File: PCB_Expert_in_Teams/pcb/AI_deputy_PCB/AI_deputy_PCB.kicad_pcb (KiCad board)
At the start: 2 copper layers, 110 parts, among them IC1 DA7280-00FVC, IC2 DA7281-00FVC, IC3 DA7282-00FVC, IC4 IS31AP2005-SLS2-TR, IC5 IS31AP2005-SLS2-TR, IC6 LM25576QMH_NOPB, IC7 CYPD3177-24LQXQ, IC8 FT231XS-R, J1 Piezo Electric, J10 OUTPUT Haptic B (Neck R), J11 OUTPUT Haptic C (Back), J12 Haptic Power and GND, J13 Conn_01x02_Socket, J14 Conn_01x02_Socket, J3 Haptic Power and GND, J4 UART, J5 JST CONN from MCU, J6 JTAG, J7 JST CONN from MCU, J8 Conn_01x04_Socket, J9 OUTPUT Haptic A (Neck L), Q1 NMOS, Q2 DMP3098LSD-13, Q4 DMP3098LSD-13, U2 ESP32-WROOM-32UE

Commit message: update schematic from desktop
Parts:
- added C38: 4u7, Capacitor_SMD:C_0805_2012Metric_Pad1.18x1.45mm_HandSolder, F.Cu at (202.5, 19.4)
- added C44: 100n, Capacitor_SMD:C_0805_2012Metric_Pad1.18x1.45mm_HandSolder, F.Cu at (218.5, 20.8)
- added C45: 4u7, Capacitor_SMD:C_0805_2012Metric_Pad1.18x1.45mm_HandSolder, F.Cu at (198.6, 24.3)
- added C46: 100n, Capacitor_SMD:C_0805_2012Metric_Pad1.18x1.45mm_HandSolder, F.Cu at (218.6, 28.7)
- added C47: 4u7, Capacitor_SMD:C_0805_2012Metric_Pad1.18x1.45mm_HandSolder, F.Cu at (250.9, 49.9)
- added C48: 4u7, Capacitor_SMD:C_0805_2012Metric_Pad1.18x1.45mm_HandSolder, F.Cu at (202.5, 25.4)
- added C50: 4u7, Capacitor_SMD:C_0805_2012Metric_Pad1.18x1.45mm_HandSolder, F.Cu at (231.5, 42.3)
- added C50: 4u7, Capacitor_SMD:C_0805_2012Metric_Pad1.18x1.45mm_HandSolder, F.Cu at (202.5, 28.4)
- added C51: 100n, Capacitor_SMD:C_0805_2012Metric_Pad1.18x1.45mm_HandSolder, F.Cu at (226.3, 42.3)
- added C52: 10u, Capacitor_SMD:CP_Elec_4x5.4, F.Cu at (69.2, 117.2)
- added C53: 0.1u, Capacitor_SMD:C_0805_2012Metric_Pad1.18x1.45mm_HandSolder, F.Cu at (75.6, 117.2)
- added C54: 2.2u, Capacitor_SMD:C_0805_2012Metric_Pad1.18x1.45mm_HandSolder, F.Cu at (73.9, 123.3)
- added C55: 2.2u, Capacitor_SMD:C_0805_2012Metric_Pad1.18x1.45mm_HandSolder, F.Cu at (69.3, 123.3)
- added C56: 2.2u, Capacitor_SMD:C_0805_2012Metric_Pad1.18x1.45mm_HandSolder, F.Cu at (64.4, 133.4)
- added C57: 2.2u, Capacitor_SMD:C_0805_2012Metric_Pad1.18x1.45mm_HandSolder, F.Cu at (64.4, 126.6)
- added C58: 10u, Capacitor_SMD:CP_Elec_4x5.4, F.Cu at (88.2, 114.4)
- added C59: 0.1u, Capacitor_SMD:C_0805_2012Metric_Pad1.18x1.45mm_HandSolder, F.Cu at (82.1, 114.9)
- added C6: 10uF, Capacitor_SMD:C_0805_2012Metric_Pad1.18x1.45mm_HandSolder, F.Cu at (209.3, 33.2)
- added C60: 10u, Capacitor_SMD:CP_Elec_4x5.4, F.Cu at (97.4, 120.6)
- added C61: 0.1u, Capacitor_SMD:C_0805_2012Metric_Pad1.18x1.45mm_HandSolder, F.Cu at (90.8, 120.6)
- added IC9: PCM5102APWR, EXT_AI_DEPUTY_Library:SOP65P640X120-20N, F.Cu at (80.3, 124.5)
- added J16: Conn_01x01_Pin, TestPoint:TestPoint_Pad_4.0x4.0mm, F.Cu at (264.0, 33.0)
- added J17: Conn_01x01_Pin, TestPoint:TestPoint_Pad_4.0x4.0mm, F.Cu at (252.0, 33.0)
- added J2: 2171790001, EXT_AI_DEPUTY_Library:MOLEX_2171790001, F.Cu at (234.3, 33.4)
- added R37: R, Resistor_SMD:R_0805_2012Metric_Pad1.20x1.40mm_HandSolder, F.Cu at (217.4, 26.0)
- added R38: 27, Resistor_SMD:R_0805_2012Metric_Pad1.20x1.40mm_HandSolder, F.Cu at (228.1, 20.8)
- added R39: 100k, Resistor_SMD:R_0805_2012Metric_Pad1.20x1.40mm_HandSolder, F.Cu at (208.6, 22.4)
- added R40: 100k, Resistor_SMD:R_0805_2012Metric_Pad1.20x1.40mm_HandSolder, F.Cu at (209.3, 28.2)
- added R41: 10k, Resistor_SMD:R_0805_2012Metric_Pad1.20x1.40mm_HandSolder, F.Cu at (103.8, 120.7)
- added R42: 470, Resistor_SMD:R_0805_2012Metric_Pad1.20x1.40mm_HandSolder, F.Cu at (68.6, 132.5)
- added R43: 470, Resistor_SMD:R_0805_2012Metric_Pad1.20x1.40mm_HandSolder, F.Cu at (68.7, 127.7)
- added S1: 430773034825, EXT_AI_DEPUTY_Library:430773034825, F.Cu at (132.7, 50.0)
- added S2: 430773034825, EXT_AI_DEPUTY_Library:430773034825, F.Cu at (185.9, 48.5)
- C41: value 4u7 -> 0.1u
- C42: value 100n -> 10u; footprint Capacitor_SMD:C_0805_2012Metric_Pad1.18x1.45mm_HandSolder -> Capacitor_SMD:CP_Elec_4x5.4
- moved C41 178.7 mm to (77.2, 132.3), turned to 90 degrees
- moved C1 172.8 mm to (258.6, 86.1)
- moved R3 172.3 mm to (263.4, 86.1)
- moved C42 168.4 mm to (83.9, 132.2)
- moved Q1 153.3 mm to (263.2, 80.6)
- moved R35 126.7 mm to (251.9, 62.4)
- moved C3 118.9 mm to (189.0, 41.8)
- moved R4 104.0 mm to (139.4, 46.3), turned to -90 degrees
- moved R36 89.7 mm to (246.7, 60.6)
- moved D1 82.5 mm to (145.1, 31.5), turned to 180 degrees
- moved R8 74.1 mm to (140.3, 31.5)
- moved C24 72.2 mm to (166.8, 114.4), turned to -90 degrees
- moved C25 69.7 mm to (168.8, 77.2), turned to -90 degrees
- moved C23 69.2 mm to (162.2, 114.4), turned to -90 degrees
- moved C49 67.8 mm to (258.0, 40.4)
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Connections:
- C3 pad 1: Net-(C3-Pad1) -> EN_ESP32
- C41 pad 1: VBUS -> GND
- C41 pad 2: GND -> +3V3
- C42 pad 1: VBUS -> +3V3
- R2 pad 2: Net-(C3-Pad1) -> EN_ESP32
- R35 pad 1: Net-(Q2-G1) -> SAFE_PWR_EN
- R35 pad 2: SAFE_PWR_EN -> Net-(Q2-G1)
- U2 pad 27: unconnected-(U2-IO16-Pad27) -> DAC_LRCK
- U2 pad 28: unconnected-(U2-IO17-Pad28) -> DAC_DIN
- U2 pad 30: unconnected-(U2-IO18-Pad30) -> DAC_BCK
- U2 pad 31: unconnected-(U2-IO19-Pad31) -> PD_INT
- U2 pad 37: unconnected-(U2-IO23-Pad37) -> MUTE
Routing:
- net +3V3: track 276.3 -> 416.9 mm, vias 0 -> 4
- net VBUS: track 13.3 -> 95.7 mm, vias 0 -> 4
- net EN_ESP32: track 0.00 -> 63.5 mm, vias 0 -> 2
- net VDC_OUT: track 0.00 -> 43.6 mm, vias 0 -> 2
- net VBUSEN: track 0.00 -> 37.3 mm, vias 0 -> 2
- net Net-(C47-Pad2): track 0.00 -> 29.7 mm
- net SAFE_PWR_EN: track 0.00 -> 26.5 mm, vias 0 -> 2
- net MUTE: track 0.00 -> 22.2 mm
- net Net-(IC9-CAPP): track 0.00 -> 19.8 mm
- net Net-(Q2-G1): track 0.00 -> 17.6 mm
- net Net-(IC9-LDOO): track 0.00 -> 15.9 mm
- net Net-(IC7-VCCD): track 0.00 -> 14.9 mm
- net Net-(IC5-OUT-): track 0.00 -> 12.9 mm, vias 0 -> 1
- net Net-(IC4-OUT-): track 0.00 -> 12.5 mm, vias 0 -> 1
- net /PD and USBC/CC1: track 0.00 -> 12.5 mm, vias 0 -> 2
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- added copper zone on F.Cu, net VDC_OUT

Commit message: fixed small things, push from laptop
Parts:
- removed the C38 at (216.1, 51.9)
- removed the C45 at (218.6, 60.8)
- removed the C48 at (248.1, 40.5)
- removed the C50 at (231.5, 42.3)
- removed the C6 at (135.8, 36.2)
- R37: value R -> 27
- moved C6 73.4 mm to (136.0, 36.2), turned to -90 degrees
- moved C48 47.8 mm to (248.0, 40.2), turned to 180 degrees
- moved C45 41.9 mm to (218.8, 61.0), turned to -90 degrees
- moved R38 35.3 mm to (201.2, 43.8)
- moved C38 35.2 mm to (216.1, 51.9), turned to -90 degrees
- moved C44 34.1 mm to (204.2, 51.8), turned to -90 degrees
- moved C50 32.1 mm to (231.5, 42.3), turned to -90 degrees
- moved C46 29.3 mm to (200.2, 51.5), turned to -90 degrees
- moved R39 27.6 mm to (197.2, 47.5), turned to 90 degrees
- moved R40 26.4 mm to (196.8, 51.5), turned to 90 degrees
- moved R37 22.4 mm to (201.2, 41.5)
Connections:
- net Net-(IC8-USBDM) renamed -
- net Net-(IC8-USBDP) renamed +
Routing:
- net D+: track 4.36 -> 51.0 mm, vias 1 -> 2
- net D-: track 2.77 -> 48.3 mm, vias 0 -> 2
- net Net-(IC8-3V3OUT): track 0.00 -> 20.3 mm
- net +3V3: track 416.9 -> 433.5 mm
- net Net-(IC8-CBUS3): track 0.00 -> 12.5 mm, vias 0 -> 2
- net +: track 0.00 -> 4.78 mm
- net -: track 0.00 -> 4.53 mm

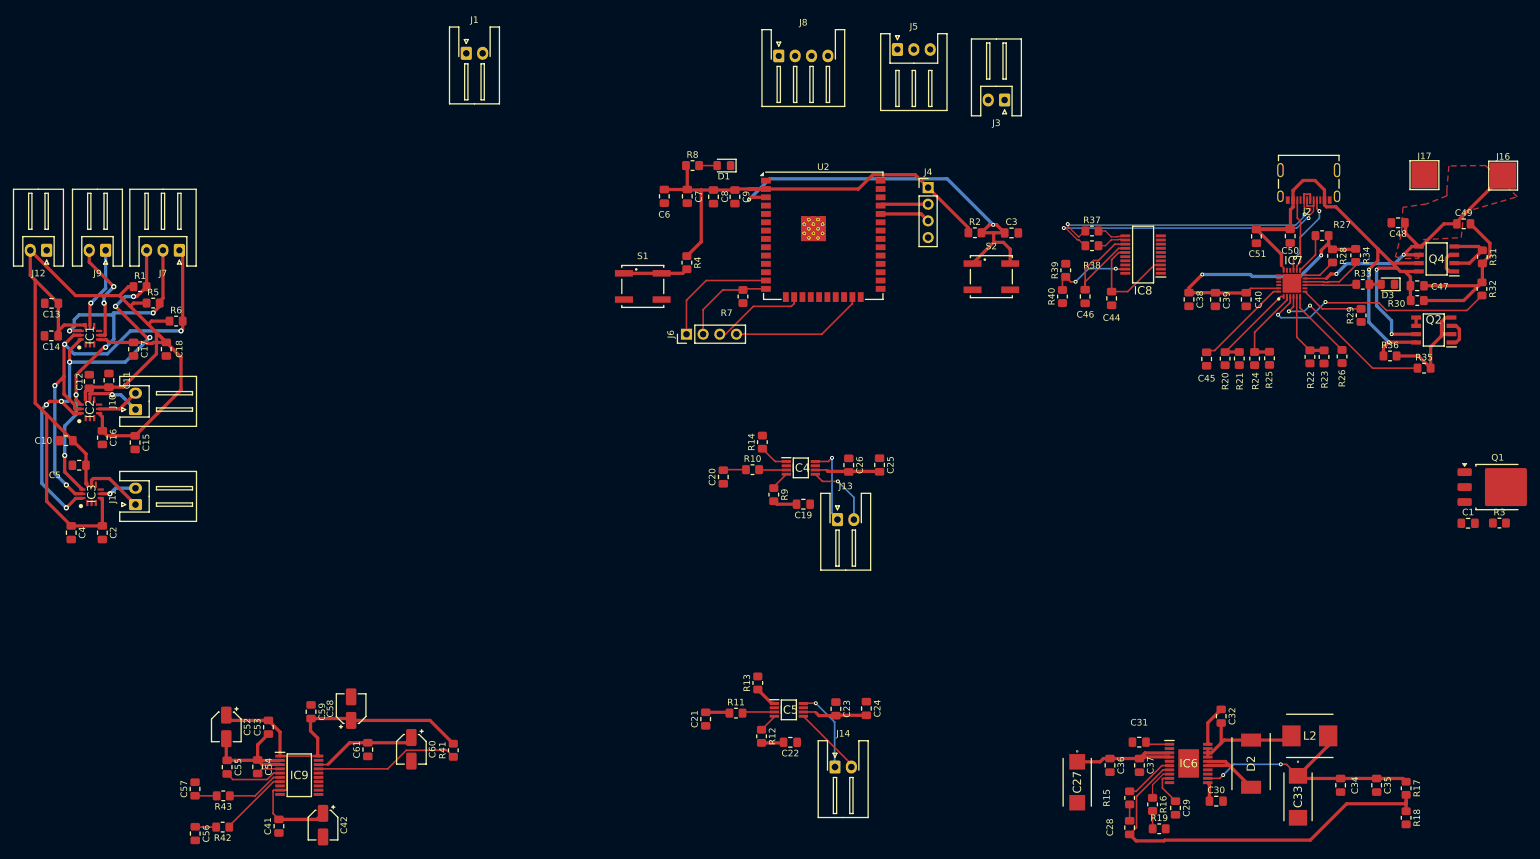
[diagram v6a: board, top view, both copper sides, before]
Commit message: pcb v0.1 plus cad render for mech students
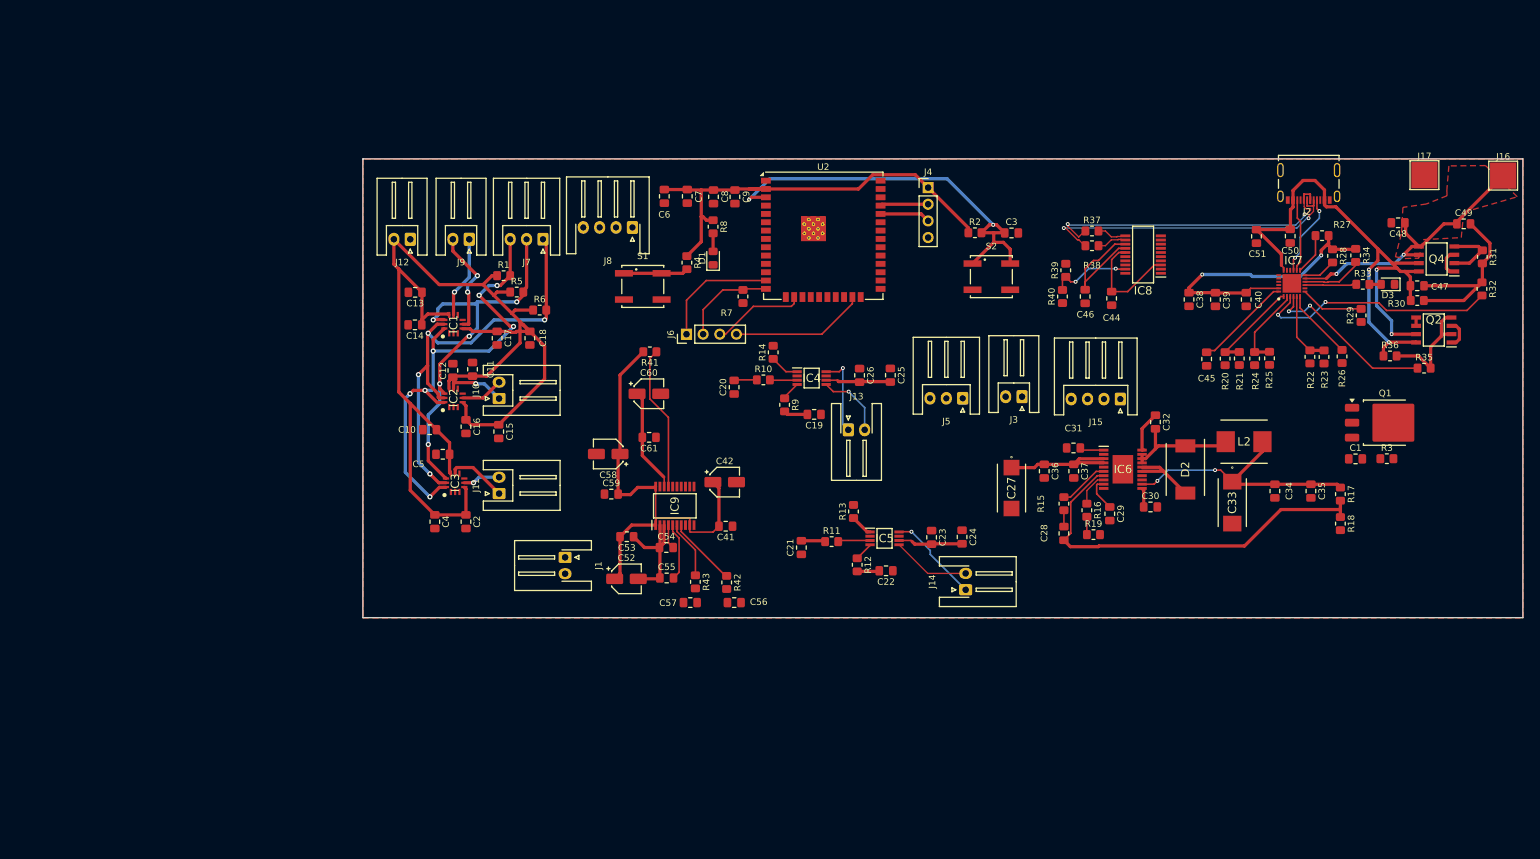
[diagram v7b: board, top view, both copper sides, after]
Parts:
- added J15: Conn_01x04_Socket, Connector_JST:JST_XH_S4B-XH-A_1x04_P2.50mm_Horizontal, F.Cu at (205.6, 67.1)
- moved C56 89.5 mm to (146.7, 98.2), turned to 0 degrees
- moved R42 85.5 mm to (145.5, 95.1), turned to -90 degrees
- moved C41 82.1 mm to (145.4, 86.5), turned to 180 degrees
- moved C57 80.7 mm to (140.0, 98.2), turned to 180 degrees
- moved C42 80.6 mm to (145.2, 79.8), turned to 0 degrees
- moved R43 79.1 mm to (140.7, 95.0), turned to -90 degrees
- moved J1 78.4 mm to (120.9, 91.3), turned to -90 degrees
- moved C55 73.0 mm to (136.4, 94.5), turned to 0 degrees
- moved C54 70.8 mm to (136.3, 89.8), turned to 0 degrees
- moved IC9 70.5 mm to (137.6, 83.4), turned to 90 degrees
- moved R41 67.8 mm to (133.8, 59.9), turned to 180 degrees
- moved C60 65.2 mm to (133.6, 66.3), turned to 0 degrees
- moved C52 65.1 mm to (130.2, 94.6), turned to 0 degrees
- moved C61 64.1 mm to (133.7, 73.0), turned to 180 degrees
- moved C53 61.9 mm to (130.3, 88.2), turned to 180 degrees
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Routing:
- net Signal Left: track 3.31 -> 0.00 mm
- net Signal Right: track 3.21 -> 0.00 mm
- net +3V3: track 433.5 -> 431.8 mm
- net Net-(IC5-OUT-): track 12.9 -> 14.2 mm
- net Net-(IC5-OUT+): track 10.8 -> 12.0 mm
- added copper zone on B.Cu, net GND
- added copper zone on F.Cu, net GND
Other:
- board outline added: 177 x 70 mm

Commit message: update after lab session with gustav saturday
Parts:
- removed C60: 10u, Capacitor_SMD:CP_Elec_4x5.4
- removed C61: 0.1u, Capacitor_SMD:C_0805_2012Metric_Pad1.18x1.45mm_HandSolder
- removed J12: Haptic Power and GND, Connector_JST:JST_XH_S2B-XH-A_1x02_P2.50mm_Horizontal
- removed J7: JST CONN from MCU, Connector_JST:JST_XH_S3B-XH-A_1x03_P2.50mm_Horizontal
- added D1: LED, LED_SMD:LED_0805_2012Metric_Pad1.15x1.40mm_HandSolder, F.Cu at (207.7, 147.9)
- added J18: Conn_01x03_Socket, Connector_PinHeader_2.54mm:PinHeader_1x03_P2.54mm_Vertical, F.Cu at (190.4, 156.9)
- added J19: Conn_01x01_Pin, TestPoint:TestPoint_Pad_4.0x4.0mm, F.Cu at (191.1, 143.5)
- added J20: Conn_01x01_Pin, TestPoint:TestPoint_Pad_4.0x4.0mm, F.Cu at (191.1, 149.6)
- added JP1: SolderJumper_2_Open, Jumper:SolderJumper-2_P1.3mm_Open_RoundedPad1.0x1.5mm, F.Cu at (203.1, 142.3)
- added JP2: SolderJumper_2_Open, Jumper:SolderJumper-2_P1.3mm_Open_RoundedPad1.0x1.5mm, F.Cu at (203.1, 145.8)
- added R44: 330, Resistor_SMD:R_0805_2012Metric_Pad1.20x1.40mm_HandSolder, F.Cu at (203.3, 152.9)
- added R45: 330, Resistor_SMD:R_0805_2012Metric_Pad1.20x1.40mm_HandSolder, F.Cu at (203.3, 155.8)
- added R46: 330, Resistor_SMD:R_0805_2012Metric_Pad1.20x1.40mm_HandSolder, F.Cu at (203.3, 158.8)
- added R47: 68, Resistor_SMD:R_0805_2012Metric_Pad1.20x1.40mm_HandSolder, F.Cu at (207.6, 144.9)
- added R48: 330, Resistor_SMD:R_0805_2012Metric_Pad1.20x1.40mm_HandSolder, F.Cu at (197.5, 135.9)
- added R49: 430, Resistor_SMD:R_0805_2012Metric_Pad1.20x1.40mm_HandSolder, F.Cu at (195.1, 156.1)
- added R50: 200, Resistor_SMD:R_0805_2012Metric_Pad1.20x1.40mm_HandSolder, F.Cu at (195.1, 159.0)
- added R51: 430, Resistor_SMD:R_0805_2012Metric_Pad1.20x1.40mm_HandSolder, F.Cu at (104.0, 136.2)
- added R52: 430, Resistor_SMD:R_0805_2012Metric_Pad1.20x1.40mm_HandSolder, F.Cu at (99.0, 136.9)
- added R53: 3.3k, Resistor_SMD:R_0805_2012Metric_Pad1.20x1.40mm_HandSolder, F.Cu at (103.5, 67.3)
- added R54: 3.3k, Resistor_SMD:R_0805_2012Metric_Pad1.20x1.40mm_HandSolder, F.Cu at (103.5, 70.2)
- added R55: 3.3k, Resistor_SMD:R_0805_2012Metric_Pad1.20x1.40mm_HandSolder, F.Cu at (103.5, 73.2)
- added R8: 10k, Resistor_SMD:R_0805_2012Metric_Pad1.20x1.40mm_HandSolder, F.Cu at (207.6, 142.0)
- C1: value 100u -> 10u
- C56, C57: value 2.2u -> 2.2n; footprint Capacitor_SMD:C_0805_2012Metric_Pad1.18x1.45mm_HandSolder -> Capacitor_SMD:C_0201_0603Metric_Pad0.64x0.40mm_HandSolder
- C6: value 10uF -> 10u
- C7: value 1uF -> 1u
- C8, C9: value 0.1uF -> 0.1u
- Q1: value NMOS -> NMOS IRLZ44NPBF; footprint Package_TO_SOT_SMD:TO-252-3_TabPin2 -> Package_TO_SOT_THT:TO-220-3_Horizontal_TabDown
- R1, R5, R6: value 4.7k -> 3.3k
- R18: value 3.01k -> 2.7k
- R23: value 2.4k -> 2k
- R26: value 2.2k -> 2k
- R27, R28, R29: value 2k2 -> 3.3k
- R3: value R -> 10k
- R33: value 10k -> 120
- R34: value 4.7k -> 51k
- R42, R43: value 470 -> 43
- moved J1 101.9 mm to (214.8, 130.9), turned to 0 degrees
- moved J10 76.6 mm to (76.8, 135.7), turned to 0 degrees
- moved J11 76.0 mm to (57.5, 135.8), turned to 0 degrees
- moved C10 62.0 mm to (58.0, 117.2)
- moved C12 62.0 mm to (61.5, 108.2)
- moved C13 62.0 mm to (55.8, 96.2)
- moved C14 62.0 mm to (55.7, 101.2)
- moved C16 62.0 mm to (63.5, 116.7)
- moved C5 62.0 mm to (60.0, 121.0)
- moved R1 62.0 mm to (69.3, 93.7)
- moved R5 62.0 mm to (71.3, 96.2)
- moved R6 62.0 mm to (74.8, 99.0)
- moved C11 62.0 mm to (64.5, 108.0)
- moved C15 62.0 mm to (68.5, 117.5)
- moved C17 62.0 mm to (68.3, 103.2)
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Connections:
- C27 pad 1: VIN -> +BATT
- C36 pad 1: VIN -> +BATT
- C37 pad 1: VIN -> +BATT
- C41 pad 1: GND -> +3V3
- C41 pad 2: +3V3 -> GND
- C52 pad 2: Net-(IC9-CAPP) -> GND
- C53 pad 1: Net-(IC9-CAPP) -> GND
- C55 pad 1: Net-(IC9-CAPP) -> GND
- IC6 pad 3: VIN -> +BATT
- IC6 pad 4: VIN -> +BATT
- IC7 pad 12: SDA -> Net-(IC7-HPI_SDA)
- IC7 pad 13: SCL -> Net-(IC7-HPI_SCL)
- IC7 pad 7: PD_INT -> Net-(IC7-HPI_INT)
- IC9 pad 13: DAC_BCK -> Net-(IC9-BCK)
- IC9 pad 14: DAC_DIN -> Net-(IC9-DIN)
- IC9 pad 15: DAC_LRCK -> Net-(IC9-LRCK)
- IC9 pad 18: Net-(IC9-LDOO) -> +3V3
- IC9 pad 3: Net-(IC9-CAPP) -> GND
- IC9 pad 8: GND -> +3V3
- IC9 pad 9: +3V3 -> GND
- Q1 pad 2: MCU PWM -> Net-(Q1-G)
- R18 pad 2: GND -> Net-(R18-Pad2)
- R23 pad 2: GND -> Net-(R23-Pad2)
- R26 pad 2: GND -> Net-(R26-Pad2)
- R27 pad 2: SCL -> Net-(IC7-HPI_SCL)
- R28 pad 2: SDA -> Net-(IC7-HPI_SDA)
- R29 pad 2: PD_INT -> Net-(IC7-HPI_INT)
- R3 pad 1: MCU PWM -> Net-(Q1-G)
- R42 pad 1: OUTR -> Net-(R42-Pad1)
- R43 pad 1: OUTL -> Net-(R43-Pad1)
- U2 pad 10: Signal Left -> Net-(JP2-A)
- U2 pad 11: Signal Right -> Net-(JP1-A)
- U2 pad 29: unconnected-(U2-IO5-Pad29) -> BT_LINK
- U2 pad 8: unconnected-(U2-IO32-Pad8) -> MCU PWM
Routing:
- net Net-(IC2-OUTN): track 8.87 -> 35.5 mm
- net Net-(IC2-OUTP): track 6.55 -> 32.1 mm, vias 0 -> 2
- net Signal Right: track 0.00 -> 23.7 mm, vias 0 -> 2
- net +BATT: track 0.00 -> 19.3 mm
- net VIN: track 20.6 -> 1.27 mm
- net Net-(IC9-LDOO): track 15.9 -> 0.00 mm
- net Net-(IC3-OUTN): track 9.13 -> 24.6 mm
- net MUTE: track 22.2 -> 11.6 mm
- net Net-(IC7-HPI_INT): track 0.00 -> 9.66 mm
- net PD_INT: track 9.66 -> 0.00 mm
- net Net-(IC3-OUTP): track 5.66 -> 13.8 mm
- net Net-(IC7-HPI_SCL): track 0.00 -> 6.27 mm
- net SCL: track 74.0 -> 67.8 mm
- net Net-(IC7-HPI_SDA): track 0.00 -> 5.02 mm
- net SDA: track 63.7 -> 58.7 mm
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- removed copper zone on B.Cu, net GND
- removed copper zone on F.Cu, net GND
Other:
- board outline removed
